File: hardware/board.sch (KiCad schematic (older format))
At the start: 21 parts, among them J1 Screw_Terminal_01x02, J2 Conn_ARM_JTAG_SWD_20, Q1 2SC1815, U1 FT2232D, U2 SN74AVC4T245PW, U3 SN74AVC4T245PW, U4 SN74AVC4T245PW

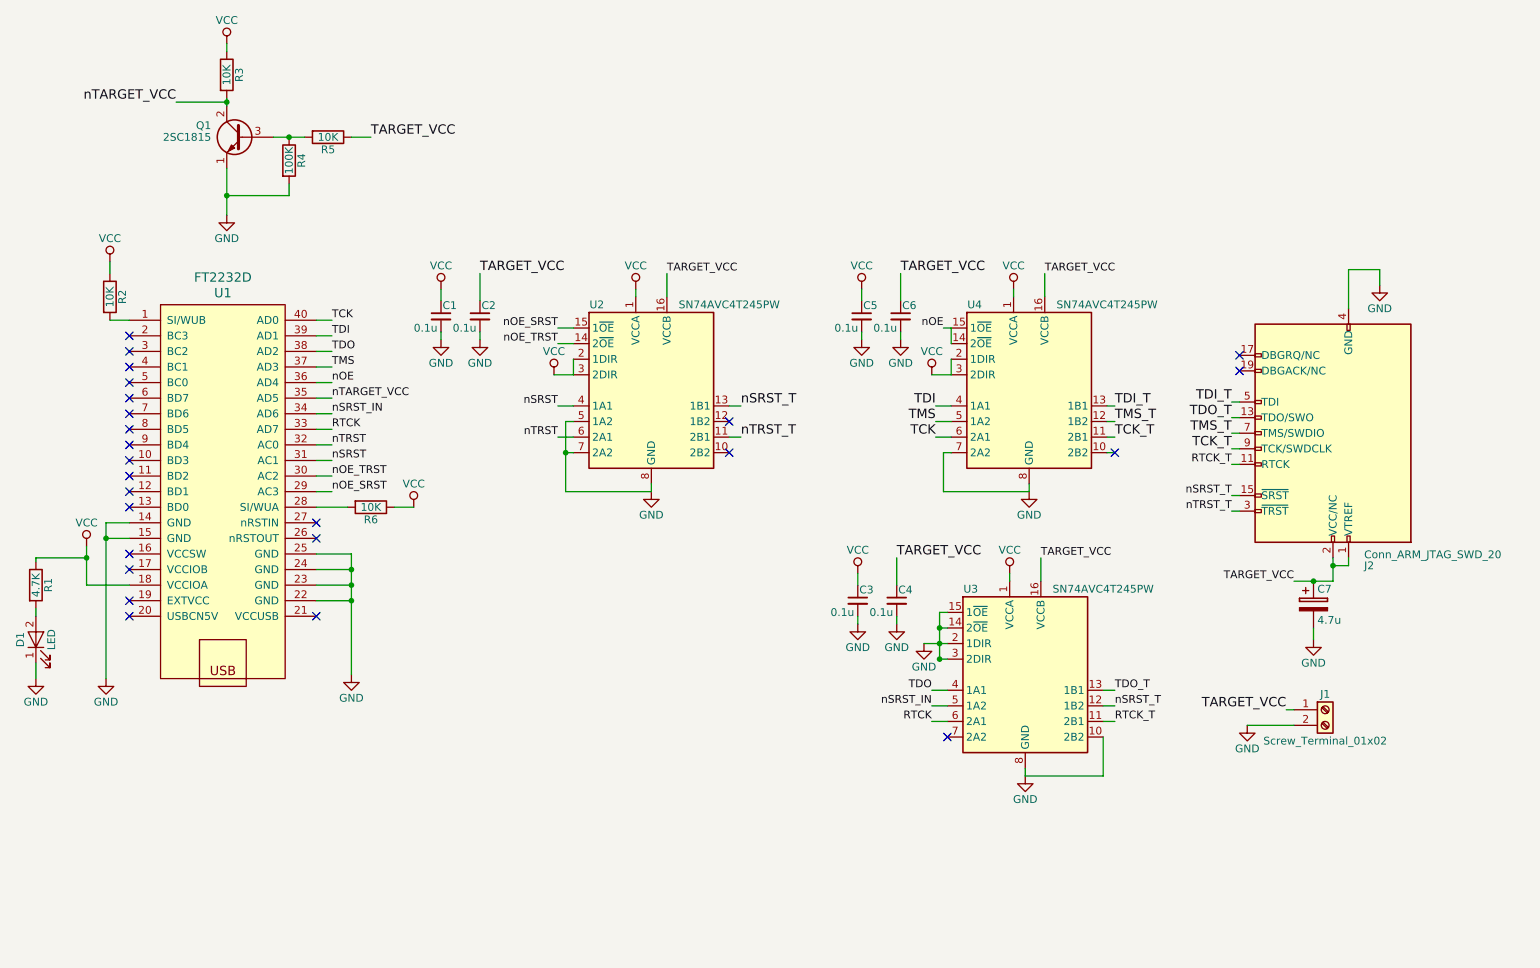
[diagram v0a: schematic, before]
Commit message: hardware: Add LEDs and register to protect undershoot
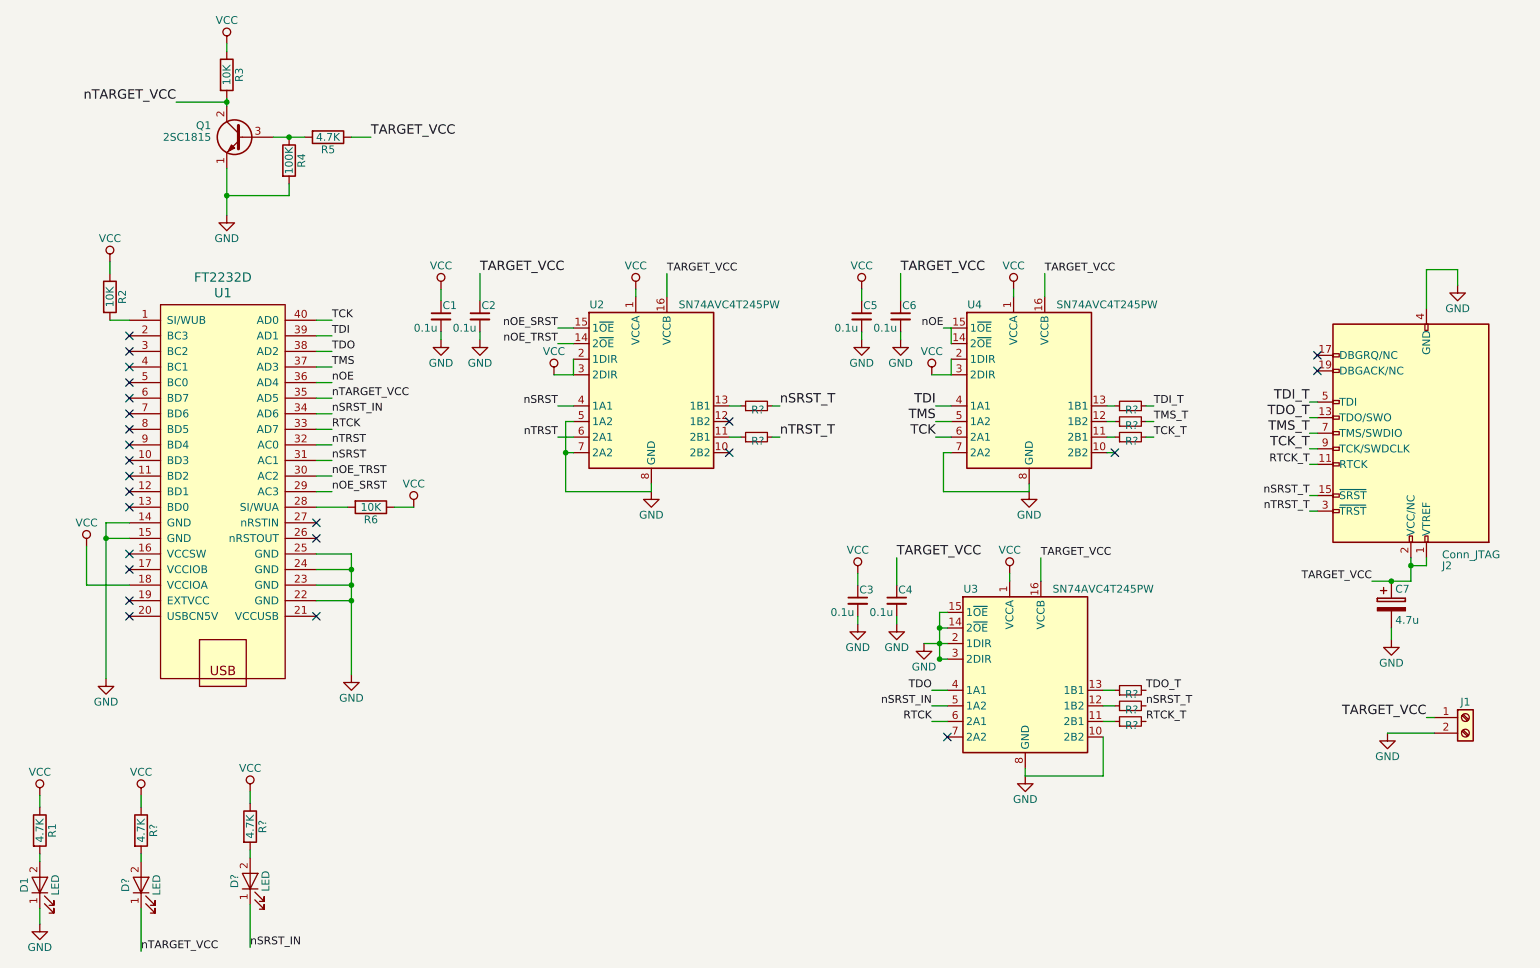
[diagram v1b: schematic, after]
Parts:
- added D? (x2): LED, symbol LED
- added R? (x8): 68, symbol R_Small
- added R? (x2): 4.7K, symbol R
- J2: value Conn_ARM_JTAG_SWD_20 -> Conn_JTAG
- R5: value 10K -> 4.7K
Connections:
- net RTCK_T: now also R?.2; no longer U3.11 (2B1)
- net TCK_T: now also R?.2; no longer U4.11 (2B1)
- net TDI_T: now also R?.2; no longer U4.13 (1B1)
- net TDO_T: now also R?.2; no longer U3.13 (1B1)
- net TMS_T: now also R?.2; no longer U4.12 (1B2)
- net VCC: now also R?.1, R?.1
- net nSRST_IN: now also D?.1 (K)
- net nSRST_T: now also R?.2, R?.2; no longer U2.13 (1B1), U3.12 (1B2)
- net nTARGET_VCC: now also D?.1 (K)
- net nTRST_T: now also R?.2; no longer U2.11 (2B1)
- new net: R?.1, U4.11 (2B1)
- new net: R?.1, U4.12 (1B2)
- new net: R?.1, U4.13 (1B1)
- new net: R?.1, U2.11 (2B1)
- new net: R?.1, U2.13 (1B1)
- new net: R?.1, U3.11 (2B1)
- new net: R?.1, U3.12 (1B2)
- new net: R?.1, U3.13 (1B1)
- new net: D?.2 (A), R?.2 (x2)
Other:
- moved on the sheet: C7, D1, J1, J2, R1

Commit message: hardware: Bump up the version to 0.1
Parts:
- C1, C2, C3, C4, C5, C6: footprint (none) -> Capacitors_SMD:C_0805_HandSoldering
- C7: value 4.7u -> 47u; footprint (none) -> Capacitors_SMD:CP_Elec_8x6.7
- D1: footprint (none) -> LEDs:LED_D3.0mm
- D2, D3: renamed from D?; footprint (none) -> LEDs:LED_D3.0mm
- J1: footprint (none) -> TerminalBlocks_Phoenix:TerminalBlock_Phoenix_MKDS1.5-2pol
- J2: footprint (none) -> Pin_Headers:Pin_Header_Straight_2x10_Pitch2.54mm
- Q1: footprint TO_SOT_Packages_THT:TO-92_Molded_Narrow -> TO_SOT_Packages_THT:TO-92_Inline_Wide
- R1, R2, R3, R5, R6: footprint (none) -> Resistors_SMD:R_0805_HandSoldering
- R10, R11, R12, R13, R14, R15, R16, R7, R8, R9: renamed from R?; footprint (none) -> Resistors_SMD:R_0805_HandSoldering
- R4: footprint (none) -> Resistors_THT:R_Axial_DIN0207_L6.3mm_D2.5mm_P10.16mm_Horizontal
- U1: footprint (none) -> AE-2232:AE-FT2232; symbol FT2232D-akizuki -> AE-FT2232D
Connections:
- net RTCK: now also U3.4 (1A1); no longer U3.6 (2A1)
- net RTCK_T: now also R14.2; no longer R16.2
- net TDO: now also U3.5 (1A2); no longer U3.4 (1A1)
- net TDO_T: now also R15.2; no longer R14.2
- net nOE_SRST: now also U2.14 (2~OE); no longer U2.15 (1~OE)
- net nOE_TRST: now also U2.15 (1~OE); no longer U2.14 (2~OE)
- net nSRST: now also U2.6 (2A1); no longer U2.4 (1A1)
- net nSRST_IN: now also U3.6 (2A1); no longer U3.5 (1A2)
- net nSRST_T: now also R10.2, R16.2; no longer R15.2, R9.2
- net nTRST: now also U2.4 (1A1); no longer U2.6 (2A1)
- net nTRST_T: now also R9.2; no longer R10.2

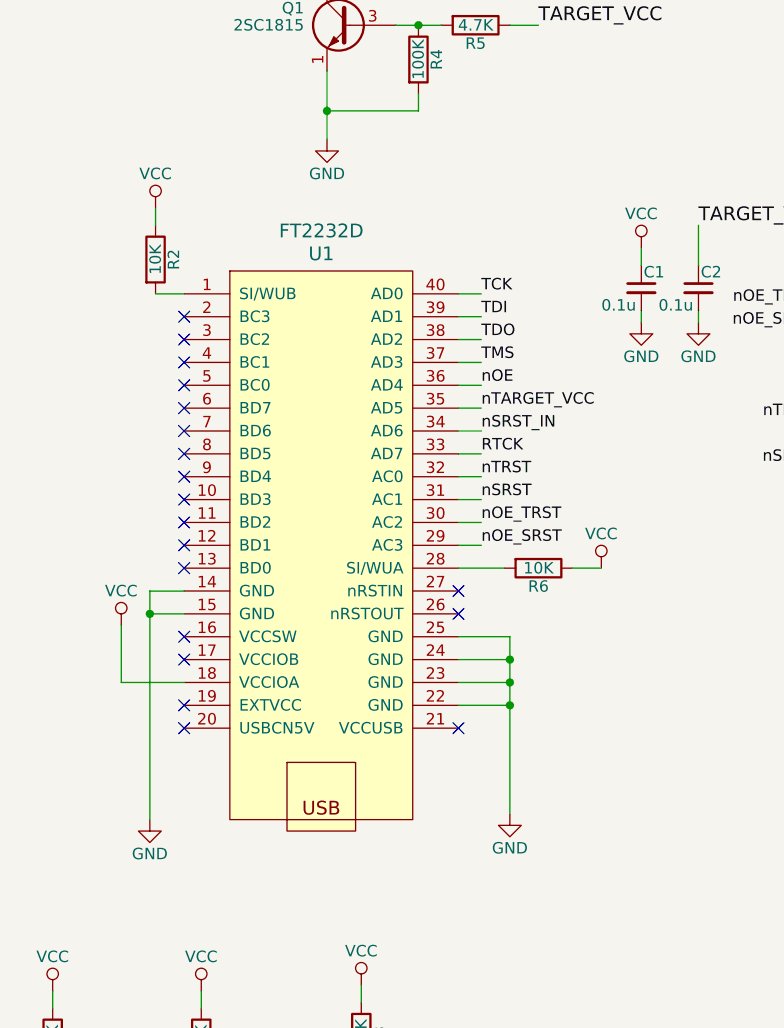
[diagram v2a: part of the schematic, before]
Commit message: hardware: schematic: Extract FT2232 to ft2232.sch
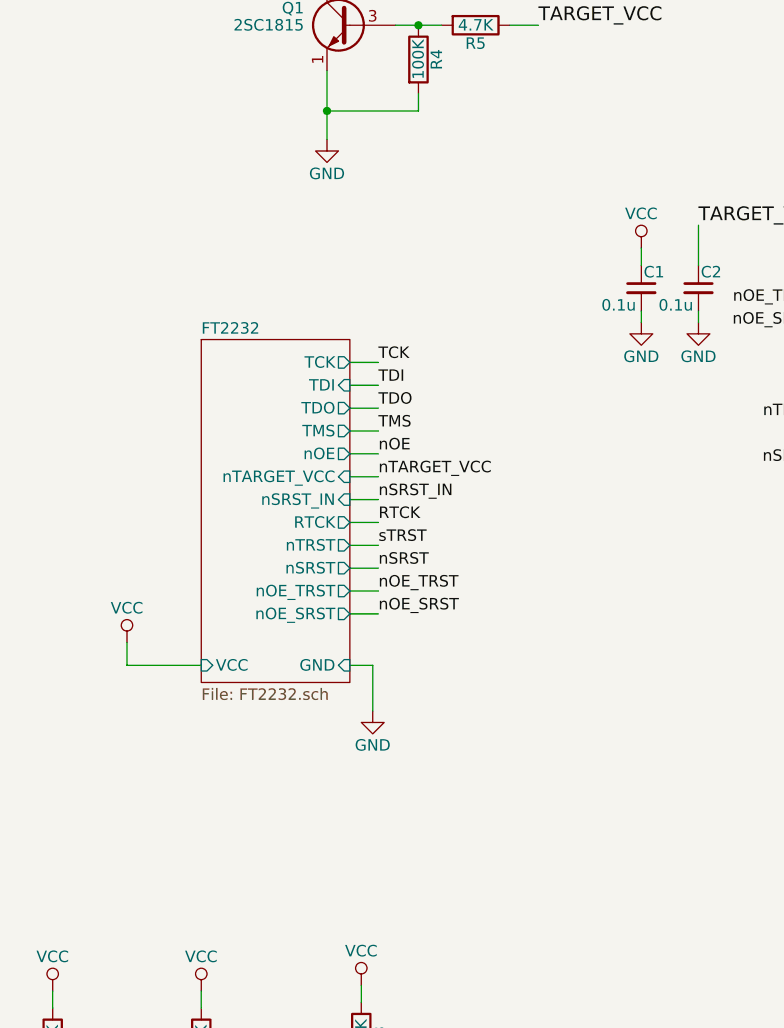
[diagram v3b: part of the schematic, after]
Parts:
- removed R2, R6: 10K, Resistors_SMD:R_0805_HandSoldering, symbol R
- removed U1: FT2232D, AE-2232:AE-FT2232, symbol AE-FT2232D
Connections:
- no-connect marks 25 -> 6
